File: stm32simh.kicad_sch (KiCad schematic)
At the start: 0 parts

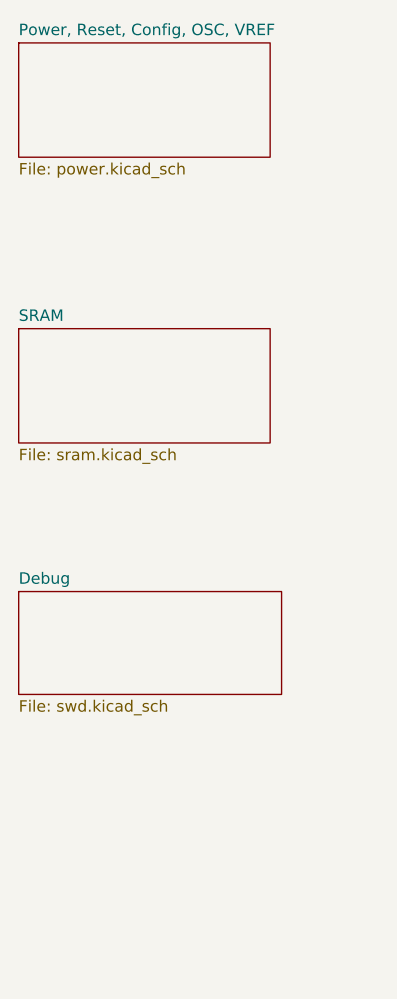
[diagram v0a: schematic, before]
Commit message: add SDIO
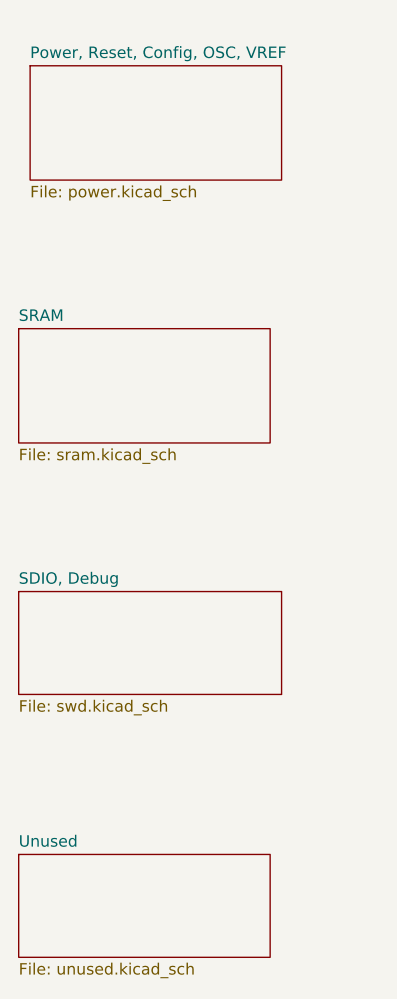
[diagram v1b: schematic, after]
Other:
- sheet Debug renamed SDIO, Debug
- added sheet Unused (unused.kicad_sch)
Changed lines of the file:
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@@
+	)
+	(sheet
+		(at 41.91 135.89)
+		(size 27.94 11.43)
+		(fields_autoplaced yes)
+		(stroke
+			(width 0.1524)
+			(type solid)
+		)
+		(fill
+			(color 0 0 0 0.0000)
+		)
+		(property "Sheetname" "Unused"
+			(at 41.91 135.1784 0)
+			(effects
+				(font
+					(size 1.27 1.27)
+				)
+				(justify left bottom)
+			)
+		)
+		(property "Sheetfile" "unused.kicad_sch"
+			(at 41.91 147.9046 0)
+			(effects
+				(font
+					(size 1.27 1.27)
+				)
+				(justify left top)
+			)
+		)
+		(instances
+			(project "stm32simh"
+				(path "/114c4e64-0fac-420a-8fa7-2afba1510345"
+					(page "5")
+				)
+			)
+		)
 	)
 	(sheet
@@
 			(color 0 0 0 0.0000)
 		)
-		(property "Sheetname" "Debug"
+		(property "Sheetname" "SDIO, Debug"
 			(at 41.91 105.9684 0)
 			(effects
@@
 	)
 	(sheet
-		(at 41.91 45.72)
+		(at 43.18 48.26)
 		(size 27.94 12.7)
 		(fields_autoplaced yes)
@@
 		)
 		(property "Sheetname" "Power, Reset, Config, OSC, VREF"
-			(at 41.91 45.0084 0)
+			(at 43.18 47.5484 0)
 			(effects
 				(font
@@
 		)
 		(property "Sheetfile" "power.kicad_sch"
-			(at 41.91 59.0046 0)
+			(at 43.18 61.5446 0)
 			(effects
 				(font

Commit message: checkpoint
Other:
- sheet Power, Reset, Config, OSC, VREF renamed STM32 Suppler, Reset, Config, OSC, VREF
- added sheet Ethernet (ethernet.kicad_sch)
- added sheet UART, UCB VCP, VBUS (serial.kicad_sch)
- sheet SDIO, Debug ports: added ~{RESET}; removed none
- sheet STM32 Suppler, Reset, Config, OSC, VREF ports: added ~{RESET}; removed none
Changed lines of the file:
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@@
 		(rev "1")
+	)
+	(junction
+		(at 82.55 83.82)
+		(diameter 0)
+		(color 0 0 0 0)
+	)
+	(wire
+		(pts
+			(xy 82.55 111.76) (xy 82.55 83.82)
+		)
+		(stroke
+			(width 0)
+			(type default)
+		)
+	)
+	(wire
+		(pts
+			(xy 82.55 83.82) (xy 82.55 54.61)
+		)
+		(stroke
+			(width 0)
+			(type default)
+		)
+	)
+	(wire
+		(pts
+			(xy 96.52 83.82) (xy 82.55 83.82)
+		)
+		(stroke
+			(width 0)
+			(type default)
+		)
+	)
+	(wire
+		(pts
+			(xy 82.55 54.61) (xy 69.85 54.61)
+		)
+		(stroke
+			(width 0)
+			(type default)
+		)
+	)
+	(wire
+		(pts
+			(xy 69.85 111.76) (xy 82.55 111.76)
+		)
+		(stroke
+			(width 0)
+			(type default)
+		)
 	)
 	(sheet
@@
 	)
 	(sheet
+		(at 96.52 48.26)
+		(size 27.94 12.7)
+		(fields_autoplaced yes)
+		(stroke
+			(width 0.1524)
+			(type solid)
+		)
+		(fill
+			(color 0 0 0 0.0000)
+		)
+		(property "Sheetname" "UART, UCB VCP, VBUS"
+			(at 96.52 47.5484 0)
+			(effects
+				(font
+					(size 1.27 1.27)
+				)
+				(justify left bottom)
+			)
+		)
+		(property "Sheetfile" "serial.kicad_sch"
+			(at 96.52 61.5446 0)
+			(effects
+				(font
+					(size 1.27 1.27)
+				)
+				(justify left top)
+			)
+		)
+		(instances
+			(project "stm32simh"
+				(path "/114c4e64-0fac-420a-8fa7-2afba1510345"
+					(page "6")
+				)
+			)
+		)
+	)
+	(sheet
+		(at 96.52 77.47)
+		(size 27.94 12.7)
+		(fields_autoplaced yes)
+		(stroke
+			(width 0.1524)
+			(type solid)
+		)
+		(fill
+			(color 0 0 0 0.0000)
+		)
+		(property "Sheetname" "Ethernet"
+			(at 96.52 76.7584 0)
+			(effects
+				(font
+					(size 1.27 1.27)
+				)
+				(justify left bottom)
+			)
+		)
+		(property "Sheetfile" "ethernet.kicad_sch"
+			(at 96.52 90.7546 0)
+			(effects
+				(font
+					(size 1.27 1.27)
+				)
+				(justify left top)
+			)
+		)
+		(pin "~{RESET}" input
+			(at 96.52 83.82 180)
+			(effects
+				(font
+					(size 1.27 1.27)
+				)
+				(justify left)
+			)
+		)
+		(instances
+			(project "stm32simh"
+				(path "/114c4e64-0fac-420a-8fa7-2afba1510345"
+					(page "7")
+				)
+			)
+		)
+	)
+	(sheet
 		(at 41.91 77.47)
 		(size 27.94 12.7)
@@
 	(sheet
 		(at 41.91 106.68)
-		(size 29.21 11.43)
+		(size 27.94 11.43)
 		(fields_autoplaced yes)
 		(stroke
@@
 			)
 		)
+		(pin "~{RESET}" bidirectional
+			(at 69.85 111.76 0)
+			(effects
+				(font
+					(size 1.27 1.27)
+				)
+				(justify right)
+			)
+		)
 		(instances
 			(project "stm32simh"
@@
 	)
 	(sheet
-		(at 43.18 48.26)
+		(at 41.91 48.26)
 		(size 27.94 12.7)
 		(fields_autoplaced yes)
@@
 			(color 0 0 0 0.0000)
 		)
-		(property "Sheetname" "Power, Reset, Config, OSC, VREF"
-			(at 43.18 47.5484 0)
+		(property "Sheetname" "STM32 Suppler, Reset, Config, OSC, VREF"
+			(at 41.91 47.5484 0)
 			(effects
 				(font
@@
 		)
 		(property "Sheetfile" "power.kicad_sch"
-			(at 43.18 61.5446 0)
-			(effects
-				(font
-					(size 1.27 1.27)
-				)
-				(justify left top)
-			)
-		)
+			(at 41.91 61.5446 0)
+			(effects
+				(font
+					(size 1.27 1.27)
+				)
+				(justify left top)
+			)
+		)
+		(pin "~{RESET}" output
+			(at 69.85 54.61 0)
+			(effects
+				(font
+					(size 1.27 1.27)
+				)
+				(justify right)
+			)
+		)

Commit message: first stab at board layout
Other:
- sheet STM32 Suppler, Reset, Config, OSC, VREF renamed STM32 Supplies, Reset, Config, OSC, VREF
- sheet UART, UCB VCP, VBUS ports: added ~{RESET}; removed none
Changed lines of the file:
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@@
+	)
+	(junction
+		(at 82.55 54.61)
+		(diameter 0)
+		(color 0 0 0 0)
 	)
 	(junction
@@
 	(wire
 		(pts
+			(xy 82.55 54.61) (xy 96.52 54.61)
+		)
+		(stroke
+			(width 0)
+			(type default)
+		)
+	)
+	(wire
+		(pts
 			(xy 96.52 83.82) (xy 82.55 83.82)
 		)
@@
 			)
 		)
+		(pin "~{RESET}" input
+			(at 96.52 54.61 180)
+			(effects
+				(font
+					(size 1.27 1.27)
+				)
+				(justify left)
+			)
+		)
 		(instances
 			(project "stm32simh"
@@
 			(color 0 0 0 0.0000)
 		)
-		(property "Sheetname" "STM32 Suppler, Reset, Config, OSC, VREF"
+		(property "Sheetname" "STM32 Supplies, Reset, Config, OSC, VREF"
 			(at 41.91 47.5484 0)
 			(effects

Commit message: cleanups
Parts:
- added H1, H2, H3, H4: MountingHole, MountingHole:MountingHole_2.2mm_M2_ISO14580_Pad, symbol Mechanical:MountingHole
- added H6: OSHW, Symbol:OSHW-Logo_7.5x8mm_SilkScreen, symbol Mechanical:MountingHole
